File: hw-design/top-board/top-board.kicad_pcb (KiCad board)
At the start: 2 copper layers, 170 x 65.9 mm, 115 parts, among them P1 POWER_CONN, P2 BACKLIGHT, P3 BACKLIGHT, P4 BOTTOM_CONN, P5 ISP, P6 SPI_JTAG, P7 FOOTSWITCH, P8 FOOTSWITCH, Q1 2N7002, Q2 2N7002, SW1 SW_PUSH, U1 NCP1117DT33G, U2 74AHC1G00, U3 LPC1759FBD80, U4 PCA9685, Y1 10MHz

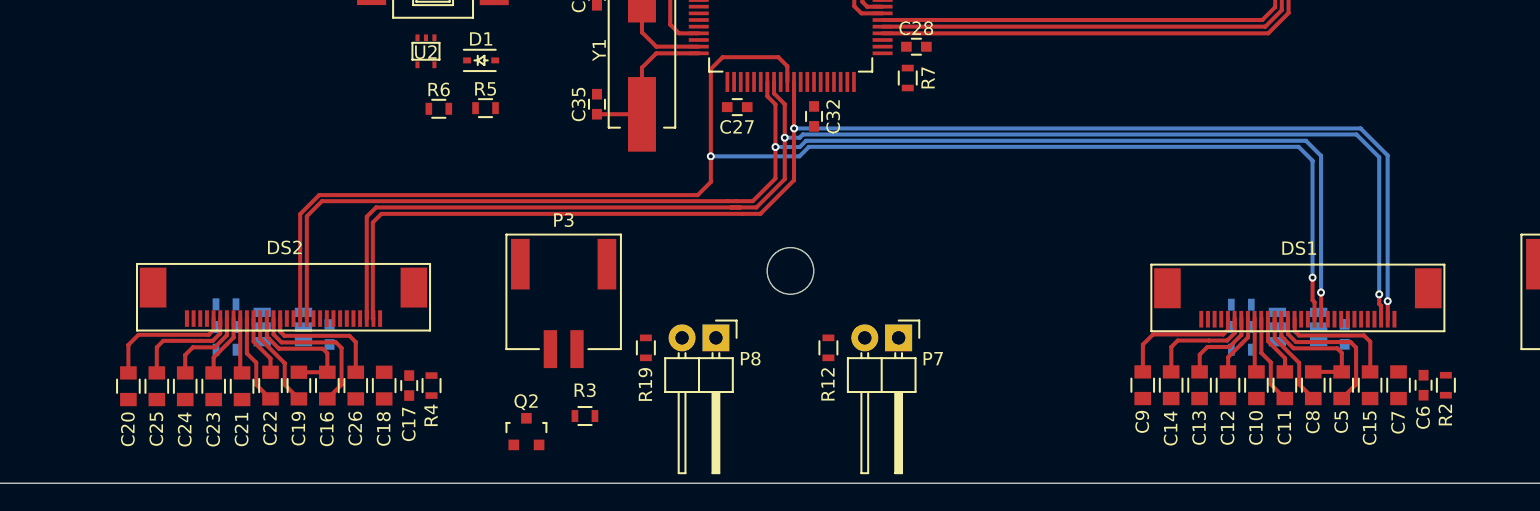
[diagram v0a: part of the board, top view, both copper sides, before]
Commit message: pcb,top-board: GLDs CS signals + footswitch signals traced
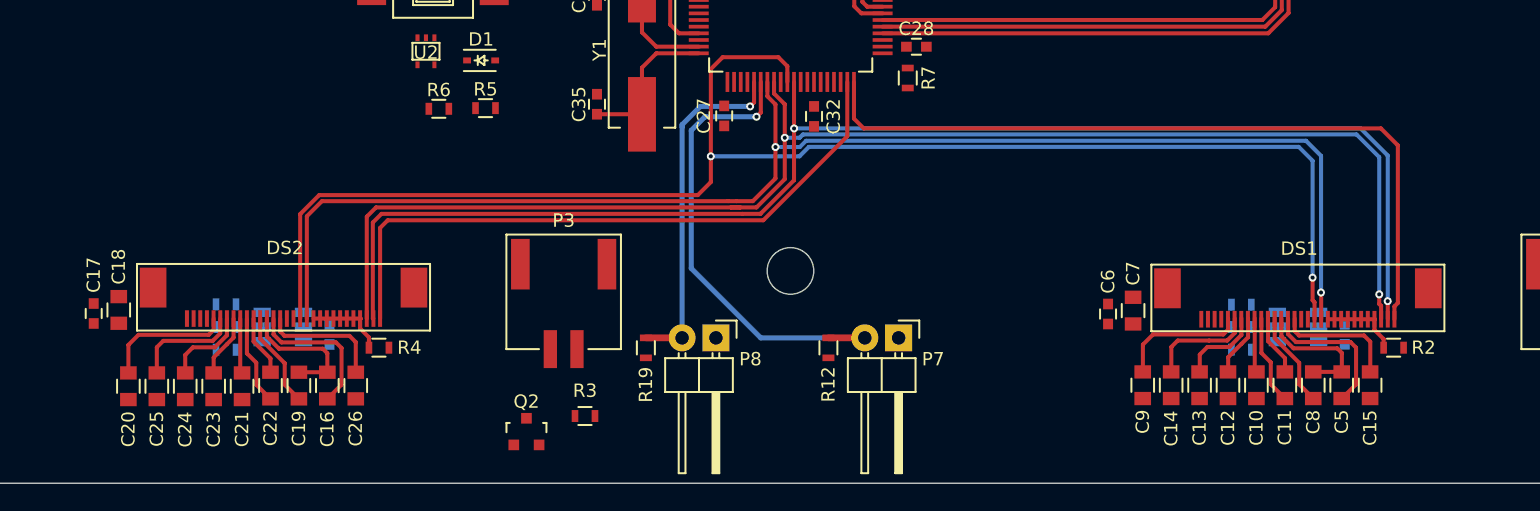
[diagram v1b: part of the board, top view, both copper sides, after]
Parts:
- moved C17 24.3 mm to (104.4, 92.3), turned to 270 degrees
- moved C6 24.3 mm to (180.5, 92.3), turned to 270 degrees
- moved C18 20.7 mm to (106.2, 92.0), turned to 270 degrees
- moved C7 20.7 mm to (182.4, 92.0), turned to 270 degrees
- moved R4 4.87 mm to (125.8, 94.8), turned to 0 degrees
- moved R2 4.83 mm to (202.0, 94.8), turned to 0 degrees
- moved C27 1.18 mm to (151.7, 77.4), turned to 270 degrees
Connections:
- U3 pad 25: GLCD1_CS -> FS2
- U3 pad 26: GLCD2_CS -> FS1
- U3 pad 39: Net-(U3-Pad39) -> GLCD2_CS
- U3 pad 40: Net-(U3-Pad40) -> GLCD1_CS
- U3 pad 51: FS2 -> Net-(U3-Pad51)
- U3 pad 52: FS1 -> Net-(U3-Pad52)
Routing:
- net GLCD1_CS: track 0.00 -> 57.6 mm
- net GLCD2_CS: track 0.00 -> 48.8 mm
- net FS1: track 0.00 -> 36.3 mm, vias 0 -> 1
- net FS2: track 0.00 -> 26.4 mm, vias 0 -> 1
- net Net-(DS2-Pad20): track 0.00 -> 6.05 mm
- net Net-(DS1-Pad20): track 0.00 -> 6.01 mm

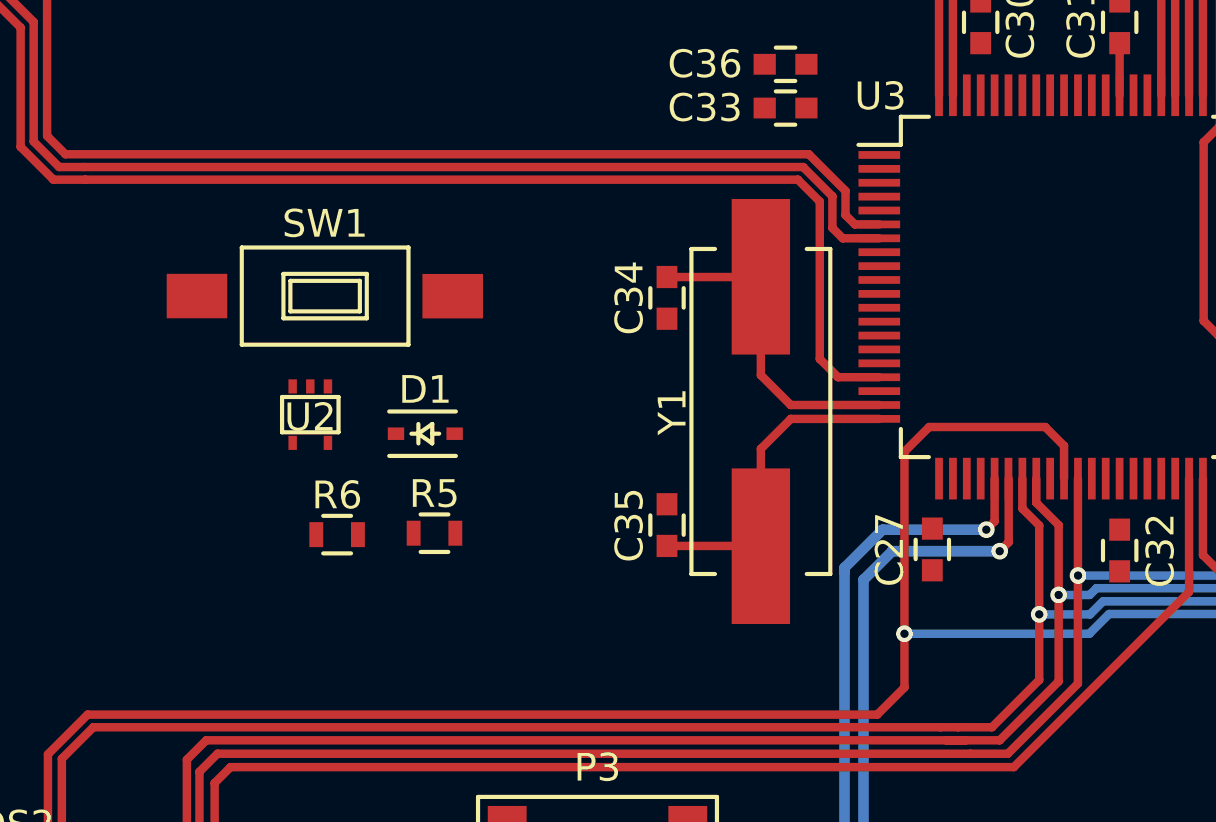
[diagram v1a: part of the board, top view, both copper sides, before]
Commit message: pcb,top-board: reset circuit done
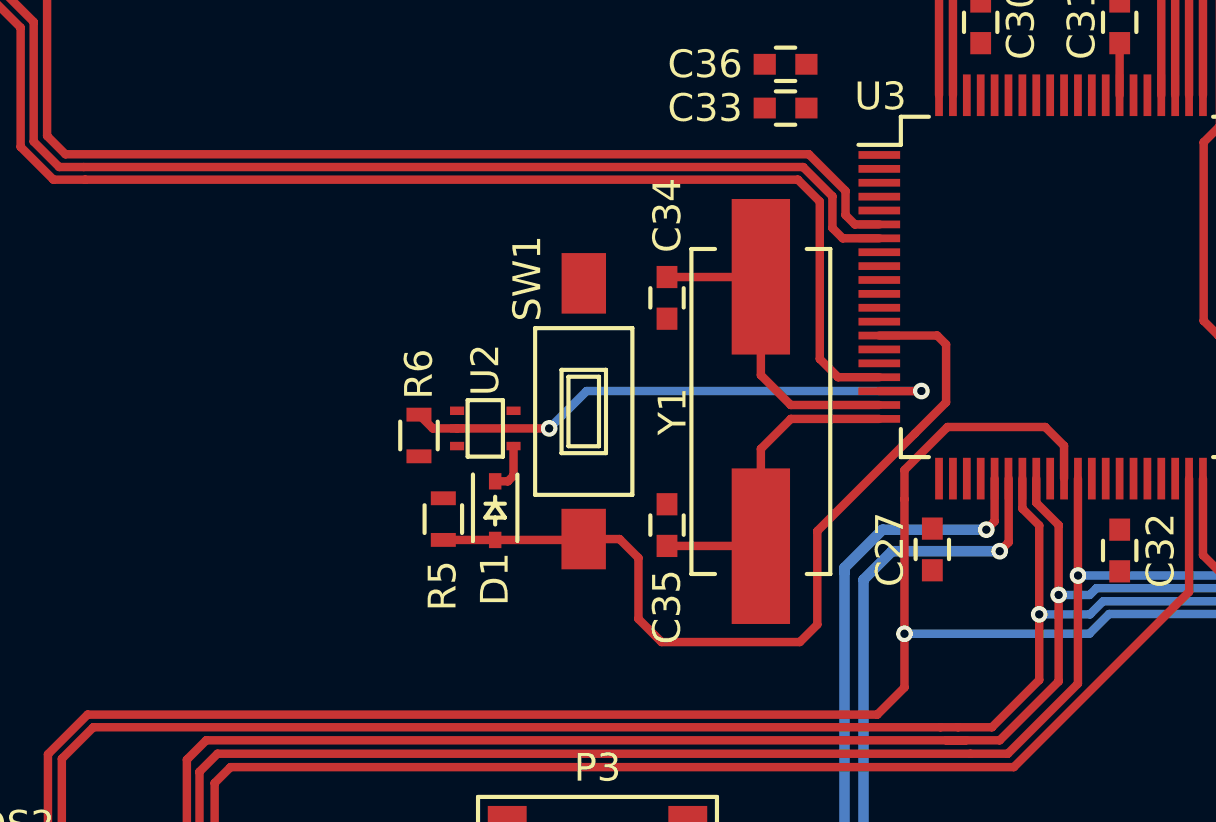
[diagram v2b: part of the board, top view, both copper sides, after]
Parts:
- moved SW1 10.2 mm to (139.2, 72.5), turned to 270 degrees
- moved U2 6.32 mm to (135.6, 73.1), turned to 0 degrees
- moved R6 4.63 mm to (133.2, 73.3), turned to 270 degrees
- moved D1 3.74 mm to (136.0, 76.0), turned to 270 degrees
- moved R5 0.60 mm to (134.1, 76.3), turned to 270 degrees
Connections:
- U3 pad 18: Net-(U3-Pad18) -> ENABLE_RESET
- U3 pad 75: ENABLE_RESET -> Net-(U3-Pad75)
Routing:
- net RESET: track 0.00 -> 31.1 mm
- net ENABLE_RESET: track 0.00 -> 20.4 mm, vias 0 -> 2
- net Net-(D1-Pad1): track 0.00 -> 1.81 mm

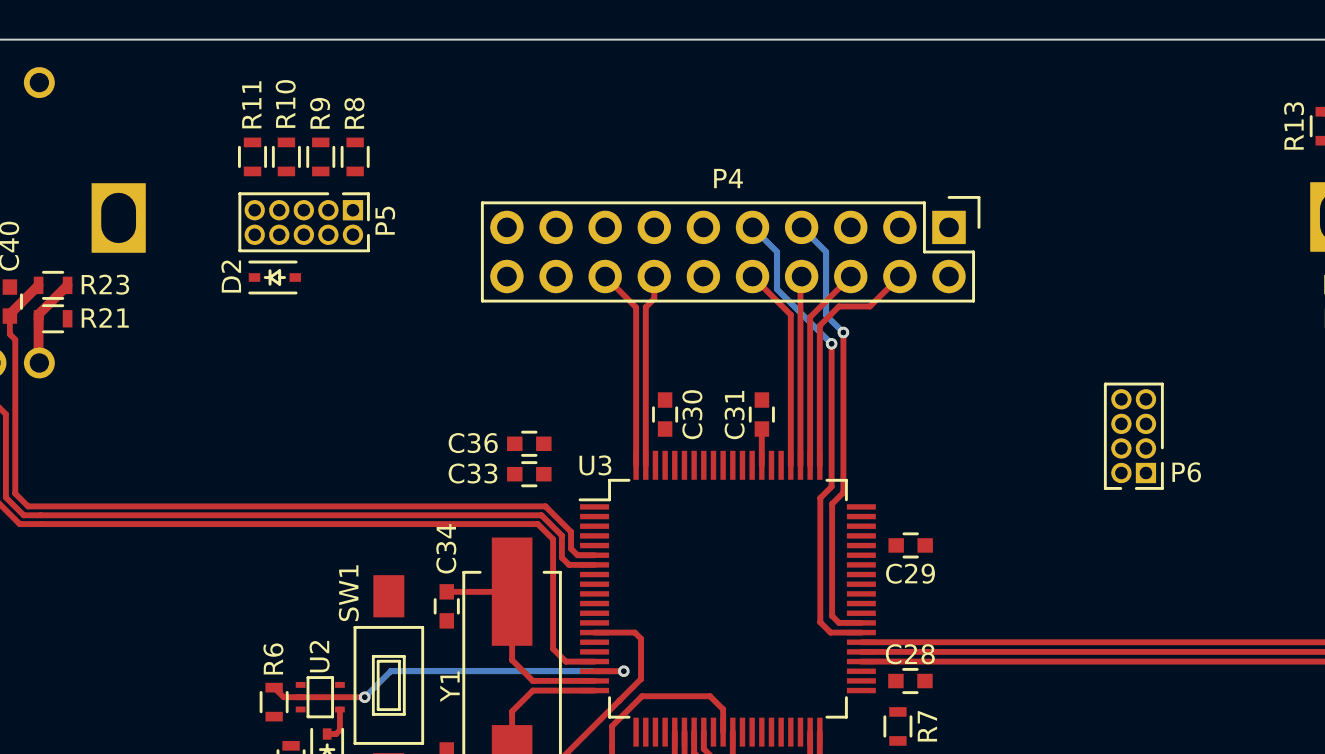
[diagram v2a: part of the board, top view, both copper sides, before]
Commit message: pcb,top-board: jtag circuit done
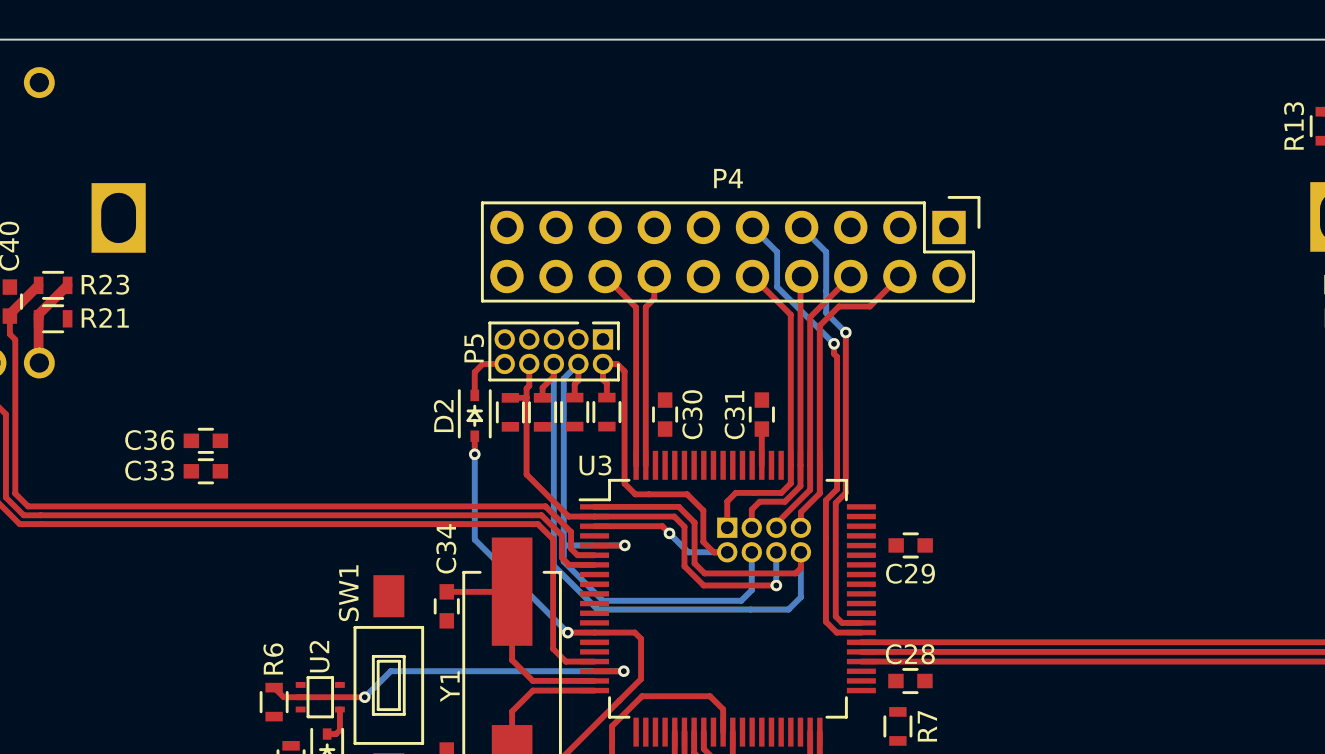
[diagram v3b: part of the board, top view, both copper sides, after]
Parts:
- P6: moved to B.Cu
- moved P6 21.8 mm to (156.7, 64.3), turned to 270 degrees
- moved R11 18.8 mm to (145.4, 58.3)
- moved R10 18.7 mm to (147.1, 58.3)
- moved R9 18.6 mm to (148.8, 58.3)
- moved R8 18.5 mm to (150.4, 58.3)
- moved C33 16.7 mm to (129.7, 61.4)
- moved C36 16.7 mm to (129.7, 59.8)
- moved P5 14.6 mm to (150.2, 54.6)
- moved D2 12.6 mm to (143.6, 58.5), turned to 270 degrees
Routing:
- net JTAG_TDO_SWO: track 0.00 -> 43.0 mm
- net JTAG_TCK_SWDCLK: track 0.00 -> 29.9 mm, vias 0 -> 1
- net JTAG_TDI: track 0.00 -> 24.9 mm, vias 0 -> 1
- net JTAG_TMS_SDWIO: track 0.00 -> 24.1 mm, vias 0 -> 1
- net RESET: track 31.1 -> 44.6 mm, vias 0 -> 2
- net SPI0_CS0_HMI: track 10.6 -> 17.0 mm
- net SPI0_CLK_HMI: track 9.79 -> 14.8 mm
- net SPI0_MOSI_HMI: track 10.6 -> 14.6 mm
- net SPI0_MISO_HMI: track 12.4 -> 16.0 mm
- net Net-(D2-Pad1): track 0.00 -> 2.93 mm

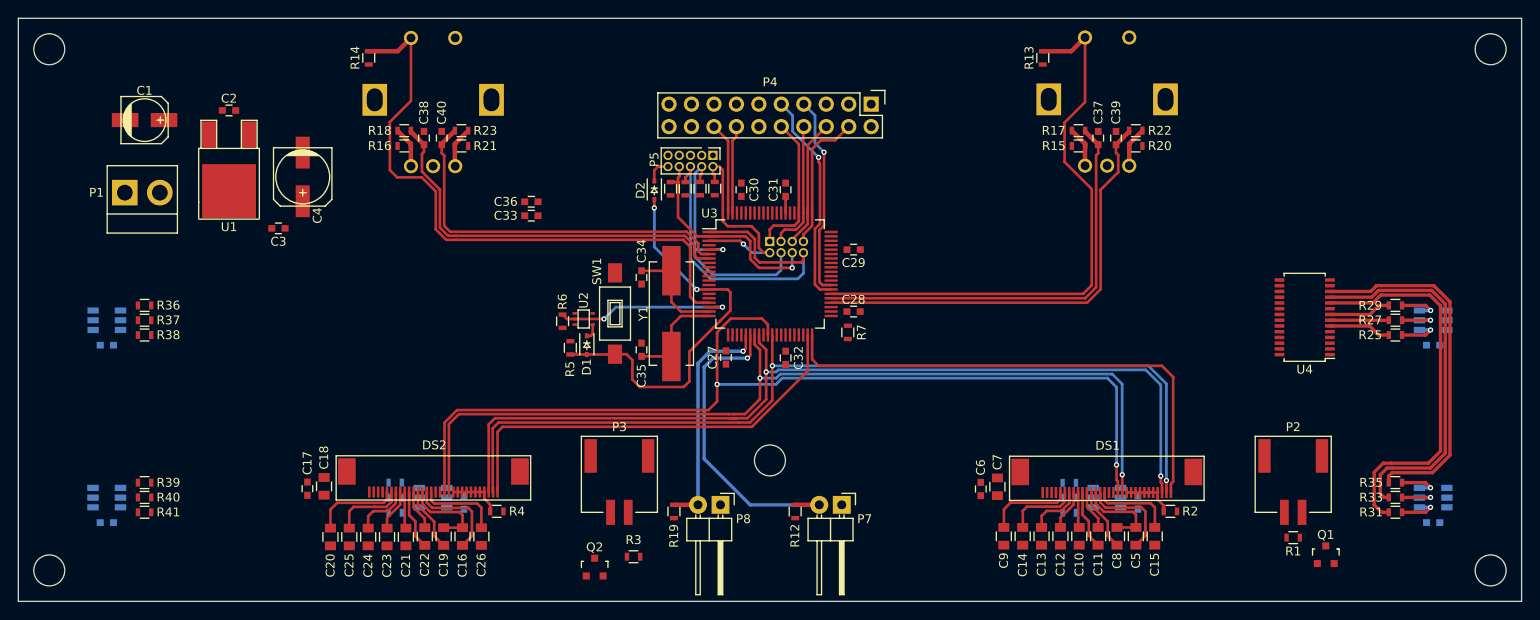
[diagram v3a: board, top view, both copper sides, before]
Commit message: pcb,top-board: some GLCDs signals redone
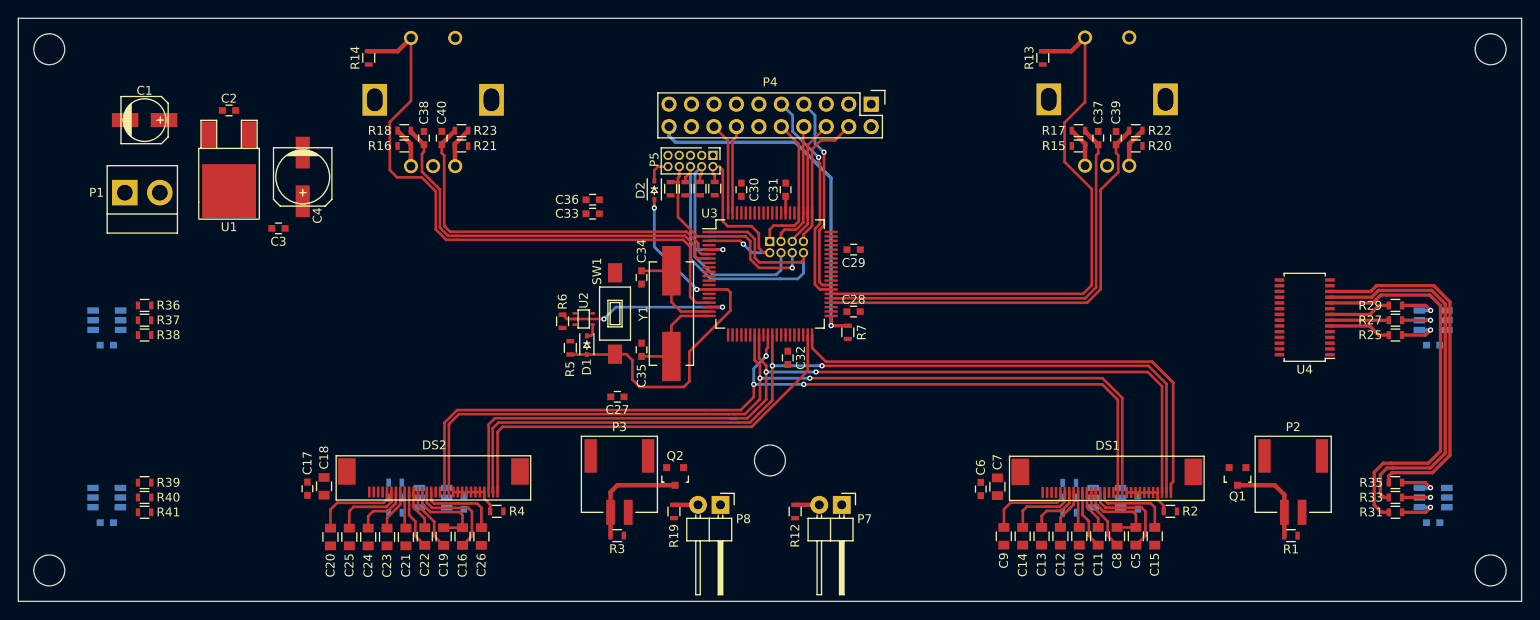
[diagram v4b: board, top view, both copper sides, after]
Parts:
- moved Q2 13.7 mm to (145.9, 90.9), turned to 180 degrees
- moved Q1 13.3 mm to (209.6, 90.9), turned to 180 degrees
- moved C27 13.1 mm to (139.4, 81.9), turned to 180 degrees
- moved C33 6.94 mm to (136.6, 61.2)
- moved C36 6.94 mm to (136.6, 59.6)
- moved R3 3.02 mm to (139.4, 97.6)
- moved R1 0.34 mm to (215.6, 97.6)
- moved C32 0.24 mm to (158.7, 77.5)
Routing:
- net HMI_ISP_ENABLE: track 0.00 -> 41.0 mm, vias 0 -> 1
- net FS1: track 36.3 -> 2.73 mm, vias 1 -> 0
- net FS2: track 26.4 -> 2.72 mm, vias 1 -> 0
- net Net-(P3-Pad1): track 0.00 -> 12.5 mm
- net Net-(P2-Pad1): track 0.00 -> 10.4 mm
- net GLCD_SI: track 113.2 -> 104.1 mm, vias 2 -> 3
- net GLCD1_CS: track 57.6 -> 59.8 mm
- net GLCD_SCL: track 105.4 -> 104.1 mm

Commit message: pcb,top-board: more LEDs signals traced
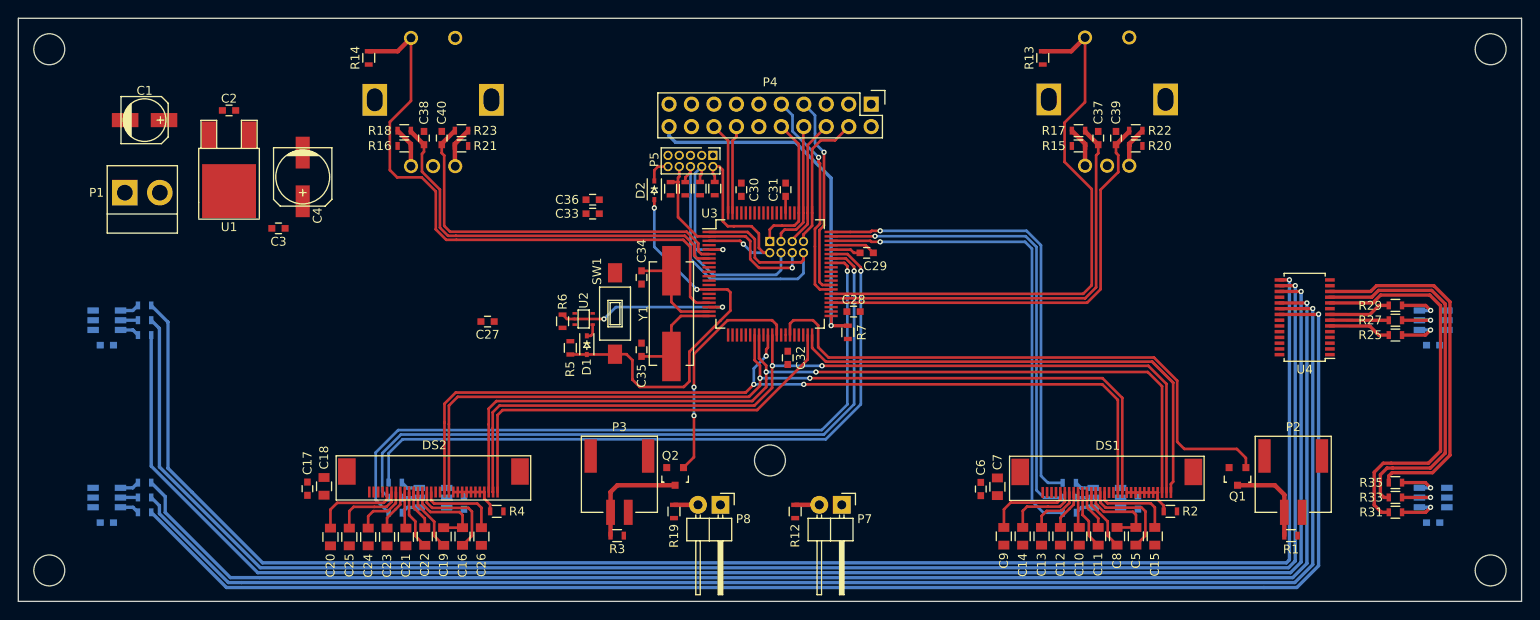
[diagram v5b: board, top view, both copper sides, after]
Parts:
- R36, R37, R38, R39, R40, R41: moved to B.Cu
- moved C27 17.0 mm to (124.7, 73.4)
- moved C29 1.52 mm to (167.6, 65.6)
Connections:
- U3 pad 32: GLCD1_BL -> GLCD2_BL
- U3 pad 35: GLCD2_BL -> GLCD1_BL
- U3 pad 53: FS2_LED_B -> FS2_LED_R
- U3 pad 55: FS2_LED_R -> FS2_LED_B
- U3 pad 58: FS1_LED_B -> FS1_LED_R
- U3 pad 60: FS1_LED_R -> FS1_LED_B
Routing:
- net Net-(R38-Pad2): track 0.00 -> 183.4 mm, vias 0 -> 1
- net Net-(R36-Pad2): track 0.00 -> 183.4 mm, vias 0 -> 1
- net Net-(R37-Pad2): track 0.00 -> 183.4 mm, vias 0 -> 1
- net Net-(R41-Pad2): track 0.00 -> 169.4 mm, vias 0 -> 1
- net Net-(R40-Pad2): track 0.00 -> 169.4 mm, vias 0 -> 1
- net Net-(R39-Pad2): track 0.00 -> 169.4 mm, vias 0 -> 1
- net FS2_LED_R: track 0.00 -> 80.6 mm, vias 0 -> 1
- net FS2_LED_G: track 0.00 -> 79.5 mm, vias 0 -> 1
- net FS2_LED_B: track 0.00 -> 78.5 mm, vias 0 -> 1
- net GLCD1_BL: track 0.00 -> 66.0 mm
- net FS1_LED_R: track 0.00 -> 55.6 mm, vias 0 -> 1
- net FS1_LED_G: track 0.00 -> 54.6 mm, vias 0 -> 1
- net FS1_LED_B: track 0.00 -> 53.3 mm, vias 0 -> 1
- net GLCD2_BL: track 0.00 -> 25.7 mm, vias 0 -> 2
- net GNDD: track 0.00 -> 5.13 mm
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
